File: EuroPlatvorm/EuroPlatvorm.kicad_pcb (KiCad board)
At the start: 4 copper layers, 21.7 x 89.8 mm, 34 parts, among them J1 Eurorack_Power_2x5, J2 USB_C_Receptacle_USB2.0, J3 Conn_01x14, J4 Conn_01x14, SW1 RST, SW2 BOOT, U1 TPS54202DDCR, U2 AMS1117-3.3, U3 USBLC6-2SC6, U4 ESP32-C6-WROOM-1-N4

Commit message: Fix USBLC6-2SC6 pin map blocker, re-route U3 area, refresh gerbers
- Symbol (platvorm.kicad_sym + embedded copy): pin4=I/O2, pin5=VBUS
  (power_in), pin6=I/O1 per ST datasheet Fig 1 (was NC/NC/VBUS)
- Schematic: VBUS label moved to pin 5 stub; USB_DM/USB_DP labels on
  pins 4/6; two no-connect flags removed
- PCB: pads 4/5/6 re-netted; USB_DP tie pads 6-1; USB_DM via-hop
  pad4 -> B.Cu -> via (135.5,127.5); VBUS jogged to pad 5 with F.Cu
  bridge through x=137.93 channel; F2-Pad2 escape wall rerouted to
  x=138.4 around J2 pad3/pad4
- 22uF value strings corrected to 6.3V (matches CL21A226MQQNNNE)
- B.Silkscreen sketch art scaled 0.984 + recentered to fit outline
  (was clipping 0.43mm past board edge)
- Zones refilled; kicad-cli DRC clean on clearance/tracks/unconnected;
  gerbers + drill + job re-exported; U3 pad nets verified in F_Cu.gbr
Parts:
- C10, C4, C5, C8: value 22uF 10V -> 22uF 6.3V
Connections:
- U3 pad 4: unconnected-(U3-NC-Pad4) -> /USB_DM
- U3 pad 5: unconnected-(U3-NC-Pad5) -> /VBUS
- U3 pad 6: /VBUS -> /USB_DP
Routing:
- net /USB_DM: track 82.6 -> 87.4 mm, vias 2 -> 3
- net /VBUS: track 17.4 -> 19.1 mm
- net /USB_DP: track 90.3 -> 91.4 mm

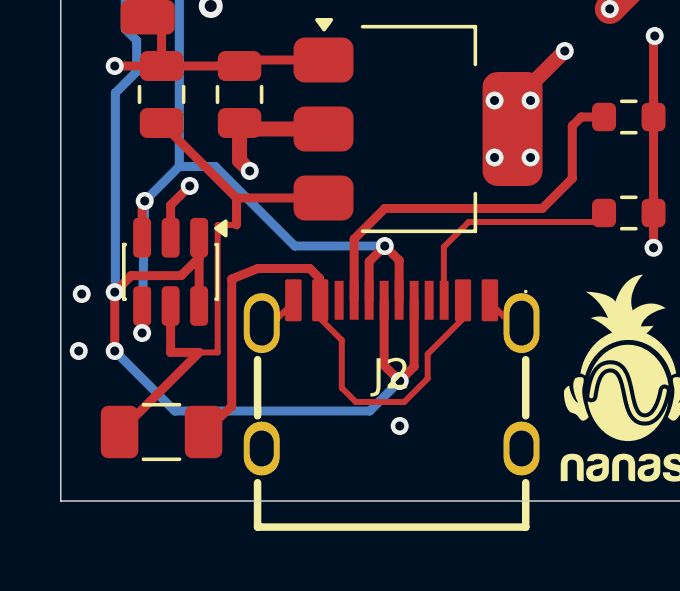
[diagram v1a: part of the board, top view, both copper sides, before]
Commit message: Re-route U3-area VBUS and F2-Pad2 escape with 45-degree geometry
- VBUS: diagonal up from (136.36,133.5) junction, straight drop, diagonal
  into the east run - replaces the 0.2mm pinch channel
- F2-Pad2 escape: swings wide east along y=133.7 into the J2 pad chain,
  freeing the pad6-to-wall corridor
- USB_DP/USB_DM far-east ends near J2 re-doglegged at 45 degrees
- Zones refilled; DRC clean (0 clearance / 0 crossing / 0 unconnected);
  gerbers + drill + job re-exported; U3 pad nets verified in F_Cu.gbr
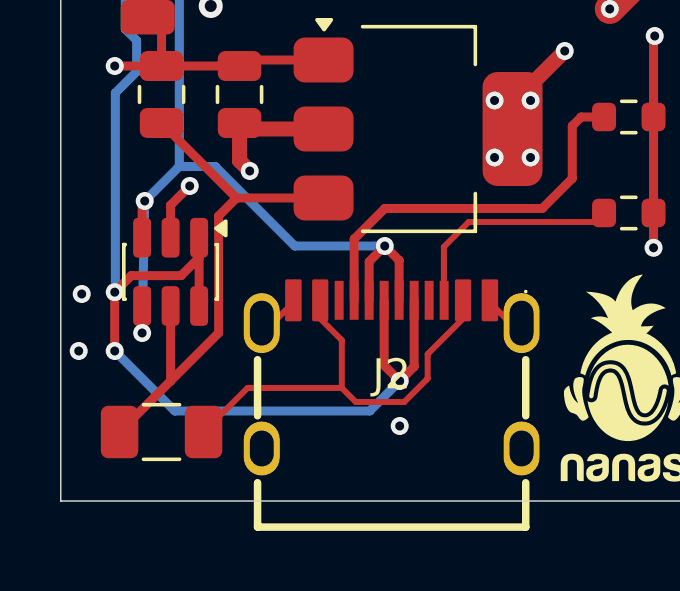
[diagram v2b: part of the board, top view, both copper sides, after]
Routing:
- net Net-(F2-Pad2): track 19.1 -> 14.9 mm
- net /VBUS: track 19.1 -> 18.3 mm
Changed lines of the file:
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@@
 	)
 	(segment
-		(start 137.93 128.3)
-		(end 138.56 128.3)
-		(width 0.2)
+		(start 134.66 135.2)
+		(end 136.3625 133.4975)
+		(width 0.3)
 		(layer "F.Cu")
 		(net "/VBUS")
 	)
 	(segment
-		(start 137.93 132.5475)
-		(end 137.93 128.3)
-		(width 0.2)
+		(start 136.3625 133.4975)
+		(end 136.3625 131)
+		(width 0.3)
 		(layer "F.Cu")
 		(net "/VBUS")
@@
 	)
 	(segment
-		(start 137.3125 132.5475)
-		(end 136.3625 132.5475)
+		(start 136.3625 133.4975)
+		(end 137.9625 131.8975)
 		(width 0.3)
 		(layer "F.Cu")
@@
 	)
 	(segment
-		(start 138.56 128.3)
+		(start 137.9625 127.9975)
 		(end 138.56 127.4)
 		(width 0.3)
@@
 	)
 	(segment
-		(start 134.66 135.2)
-		(end 137.3125 132.5475)
+		(start 137.9625 131.8975)
+		(end 137.9625 127.9975)
 		(width 0.3)
 		(layer "F.Cu")
@@
 	)
 	(segment
-		(start 137.3125 132.5475)
-		(end 137.93 132.5475)
+		(start 142.068198 133.731802)
+		(end 138.928198 133.731802)
 		(width 0.2)
 		(layer "F.Cu")
-		(net "/VBUS")
-	)
-	(segment
-		(start 136.3625 132.5475)
-		(end 136.3625 131)
-		(width 0.3)
-		(layer "F.Cu")
-		(net "/VBUS")
+		(net "Net-(F2-Pad2)")
 	)
 	(segment
@@
 		(end 141.33 131.400761)
 		(width 0.2)
-		(layer "F.Cu")
-		(net "Net-(F2-Pad2)")
-	)
-	(segment
-		(start 141.33 130.080699)
-		(end 141.33 130.81)
-		(width 0.3)
 		(layer "F.Cu")
 		(net "Net-(F2-Pad2)")
@@
 		(end 142.068198 133.731802)
 		(width 0.2)
-		(layer "F.Cu")
-		(net "Net-(F2-Pad2)")
-	)
-	(segment
-		(start 138.4 130.1)
-		(end 139.269694 129.749912)
-		(width 0.3)
-		(layer "F.Cu")
-		(net "Net-(F2-Pad2)")
-	)
-	(segment
-		(start 137.46 135.2)
-		(end 138.4 134.35)
-		(width 0.3)
 		(layer "F.Cu")
 		(net "Net-(F2-Pad2)")
@@
 	)
 	(segment
-		(start 140.999213 129.749912)
-		(end 141.33 130.080699)
-		(width 0.3)
+		(start 144.93 133.418529)
+		(end 144.148529 134.2)
+		(width 0.2)
 		(layer "F.Cu")
 		(net "Net-(F2-Pad2)")
 	)
 	(segment
-		(start 139.269694 129.749912)
-		(end 140.999213 129.749912)
-		(width 0.3)
-		(layer "F.Cu")
-		(net "Net-(F2-Pad2)")
-	)
-	(segment
-		(start 144.93 133.418529)
-		(end 144.148529 134.2)
+		(start 138.928198 133.731802)
+		(end 137.46 135.2)
 		(width 0.2)
 		(layer "F.Cu")
@@
 		(layer "F.Cu")
 		(net "Net-(F2-Pad2)")
-	)
-	(segment
-		(start 138.4 134.35)
-		(end 138.4 130.1)
-		(width 0.3)
-		(layer "F.Cu")
-		(net "Net-(F2-Pad2)")
